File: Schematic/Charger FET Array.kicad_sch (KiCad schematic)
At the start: 31 parts, among them Q21 CSD19531Q5A, Q22 CSD19531Q5A, Q23 CSD19531Q5A, Q24 CSD19531Q5A

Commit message: added sensors?
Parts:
- renumbered C71 to C126, C70 to C127, C69 to C128, C73 to C129, C72 to C130, C74 to C131, C75 to C132, C76 to C133, C77 to C134, C78 to C135, C79 to C136, L1 to L2, Q21 to Q27, Q22 to Q28, Q24 to Q29, Q23 to Q30, R99 to R114, R98 to R115, R97 to R116, R101 to R117, R100 to R118, R102 to R119, R103 to R120, R104 to R121, R105 to R122, R106 to R123, R108 to R124, R107 to R125, R110 to R126, R111 to R127, R112 to R128

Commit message: 1st Schematic Review
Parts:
- renumbered C126 to C129, C127 to C130, C128 to C131, C129 to C132, C130 to C133, C131 to C134, C132 to C135, C133 to C136, C134 to C137, C135 to C138, C136 to C139, R114 to R116, R115 to R117, R116 to R118, R117 to R119, R118 to R120, R119 to R121, R120 to R122, R121 to R123, R122 to R124, R123 to R125, R124 to R126, R125 to R127, R126 to R128, R127 to R129, R128 to R130

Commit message: updates
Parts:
- renumbered C129 to C130, C130 to C131, C131 to C132, C132 to C133, C133 to C134, C134 to C135, C135 to C136, C136 to C137, C137 to C138, C138 to C139, C139 to C140, R116 to R125, R117 to R126, R118 to R127, R119 to R128, R120 to R129, R121 to R130, R122 to R131, R123 to R132, R124 to R133, R125 to R134, R126 to R135, R127 to R136, R128 to R137, R129 to R138, R130 to R139

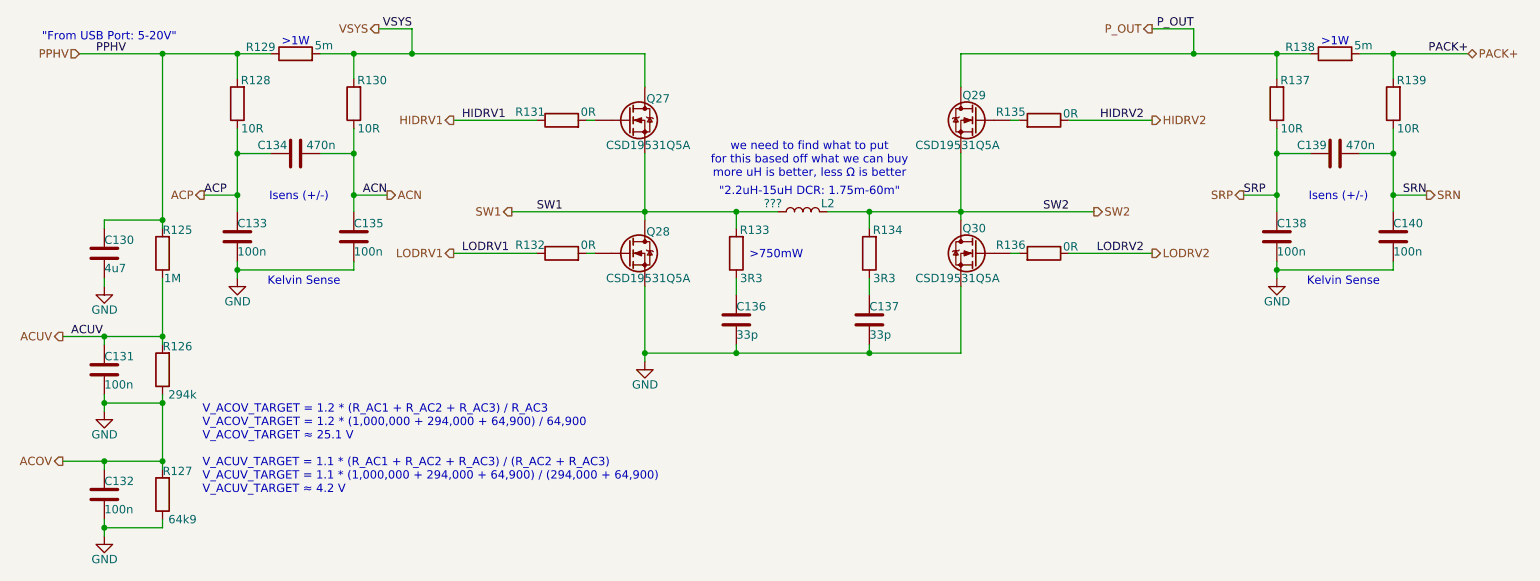
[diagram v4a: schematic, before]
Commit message: updated fuel guage
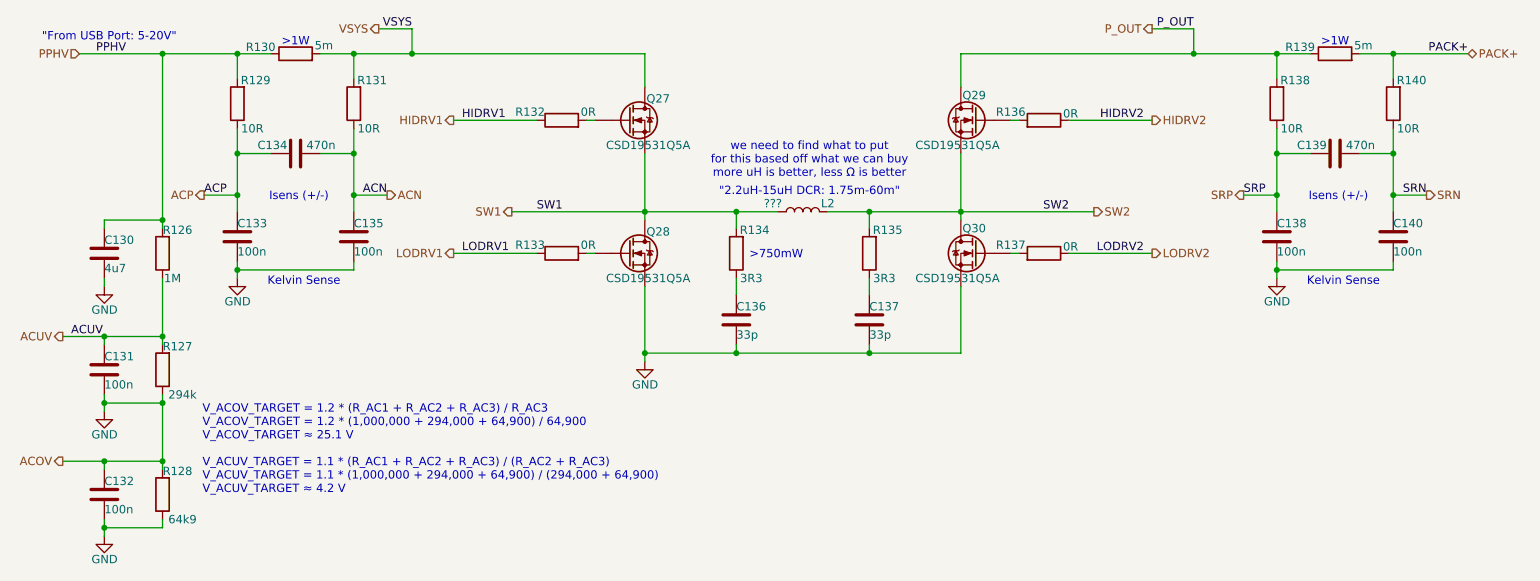
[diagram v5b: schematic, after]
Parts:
- renumbered R125 to R126, R126 to R127, R127 to R128, R128 to R129, R129 to R130, R130 to R131, R131 to R132, R132 to R133, R133 to R134, R134 to R135, R135 to R136, R136 to R137, R137 to R138, R138 to R139, R139 to R140
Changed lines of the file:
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@@
 		(on_board yes)
 		(dnp no)
-		(property "Reference" "R137"
+		(property "Reference" "R138"
 			(at 214.884 87.884 0)
 			(effects
@@
 			(project "STAR"
 				(path "/fc8533bc-25dd-4c20-9b4c-ffebebd6739b/ec72a35b-e7f2-4422-8859-60e9fb848154/9fb42b36-af5a-430a-ae71-09fe6d8fbe9c"
-					(reference "R137")
+					(reference "R138")
 					(unit 1)
 				)
@@
 		(on_board yes)
 		(dnp no)
-		(property "Reference" "R131"
+		(property "Reference" "R132"
 			(at 98.044 92.71 90)
 			(effects
@@
 			(project "STAR"
 				(path "/fc8533bc-25dd-4c20-9b4c-ffebebd6739b/ec72a35b-e7f2-4422-8859-60e9fb848154/9fb42b36-af5a-430a-ae71-09fe6d8fbe9c"
-					(reference "R131")
+					(reference "R132")
 					(unit 1)
 				)
@@
 		(on_board yes)
 		(dnp no)
-		(property "Reference" "R126"
+		(property "Reference" "R127"
 			(at 44.196 128.524 0)
 			(effects
@@
 			(project "STAR"
 				(path "/fc8533bc-25dd-4c20-9b4c-ffebebd6739b/ec72a35b-e7f2-4422-8859-60e9fb848154/9fb42b36-af5a-430a-ae71-09fe6d8fbe9c"
-					(reference "R126")
+					(reference "R127")
 					(unit 1)
 				)
@@
 		(on_board yes)
 		(dnp no)
-		(property "Reference" "R128"
+		(property "Reference" "R129"
 			(at 56.134 87.884 0)
 			(effects
@@
 			(project "STAR"
 				(path "/fc8533bc-25dd-4c20-9b4c-ffebebd6739b/ec72a35b-e7f2-4422-8859-60e9fb848154/9fb42b36-af5a-430a-ae71-09fe6d8fbe9c"
-					(reference "R128")
+					(reference "R129")
 					(unit 1)
 				)
@@
 		(on_board yes)
 		(dnp no)
-		(property "Reference" "R127"
+		(property "Reference" "R128"
 			(at 44.196 147.574 0)
 			(effects
@@
 			(project "STAR"
 				(path "/fc8533bc-25dd-4c20-9b4c-ffebebd6739b/ec72a35b-e7f2-4422-8859-60e9fb848154/9fb42b36-af5a-430a-ae71-09fe6d8fbe9c"
-					(reference "R127")
+					(reference "R128")
 					(unit 1)
 				)
@@
 		(on_board yes)
 		(dnp no)
-		(property "Reference" "R139"
+		(property "Reference" "R140"
 			(at 232.664 87.884 0)
 			(effects
@@
 			(project "STAR"
 				(path "/fc8533bc-25dd-4c20-9b4c-ffebebd6739b/ec72a35b-e7f2-4422-8859-60e9fb848154/9fb42b36-af5a-430a-ae71-09fe6d8fbe9c"
-					(reference "R139")
+					(reference "R140")
 					(unit 1)
 				)
@@
 		(on_board yes)
 		(dnp no)
-		(property "Reference" "R130"
+		(property "Reference" "R131"
 			(at 73.914 87.884 0)
 			(effects
@@
 			(project "STAR"
 				(path "/fc8533bc-25dd-4c20-9b4c-ffebebd6739b/ec72a35b-e7f2-4422-8859-60e9fb848154/9fb42b36-af5a-430a-ae71-09fe6d8fbe9c"
-					(reference "R130")
+					(reference "R131")
 					(unit 1)
 				)
@@
 		(on_board yes)
 		(dnp no)
-		(property "Reference" "R135"
+		(property "Reference" "R136"
 			(at 171.45 92.71 90)
 			(effects
@@
 			(project "STAR"
 				(path "/fc8533bc-25dd-4c20-9b4c-ffebebd6739b/ec72a35b-e7f2-4422-8859-60e9fb848154/9fb42b36-af5a-430a-ae71-09fe6d8fbe9c"
-					(reference "R135")
+					(reference "R136")
 					(unit 1)
 				)
@@
 		(on_board yes)
 		(dnp no)
-		(property "Reference" "R138"
+		(property "Reference" "R139"
 			(at 215.646 82.804 90)
 			(effects
@@
 			(project "STAR"
 				(path "/fc8533bc-25dd-4c20-9b4c-ffebebd6739b/ec72a35b-e7f2-4422-8859-60e9fb848154/9fb42b36-af5a-430a-ae71-09fe6d8fbe9c"
-					(reference "R138")
+					(reference "R139")
 					(unit 1)
 				)
@@
 		(on_board yes)
 		(dnp no)
-		(property "Reference" "R129"
+		(property "Reference" "R130"
 			(at 56.896 82.804 90)
 			(effects
@@
 			(project "STAR"
 				(path "/fc8533bc-25dd-4c20-9b4c-ffebebd6739b/ec72a35b-e7f2-4422-8859-60e9fb848154/9fb42b36-af5a-430a-ae71-09fe6d8fbe9c"
-					(reference "R129")
+					(reference "R130")
 					(unit 1)
 				)
@@
 		(on_board yes)
 		(dnp no)
-		(property "Reference" "R133"
+		(property "Reference" "R134"
 			(at 132.334 110.744 0)
 			(effects
@@
 			(project "STAR"
 				(path "/fc8533bc-25dd-4c20-9b4c-ffebebd6739b/ec72a35b-e7f2-4422-8859-60e9fb848154/9fb42b36-af5a-430a-ae71-09fe6d8fbe9c"
-					(reference "R133")
+					(reference "R134")
 					(unit 1)
 				)
@@
 		(on_board yes)
 		(dnp no)
-		(property "Reference" "R125"
+		(property "Reference" "R126"
 			(at 44.196 110.744 0)
 			(effects
@@
 			(project "STAR"
 				(path "/fc8533bc-25dd-4c20-9b4c-ffebebd6739b/ec72a35b-e7f2-4422-8859-60e9fb848154/9fb42b36-af5a-430a-ae71-09fe6d8fbe9c"
-					(reference "R125")
+					(reference "R126")
 					(unit 1)
 				)
@@
 		(on_board yes)
 		(dnp no)
-		(property "Reference" "R134"
+		(property "Reference" "R135"
 			(at 152.654 110.744 0)
 			(effects
@@
 			(project "STAR"
 				(path "/fc8533bc-25dd-4c20-9b4c-ffebebd6739b/ec72a35b-e7f2-4422-8859-60e9fb848154/9fb42b36-af5a-430a-ae71-09fe6d8fbe9c"
-					(reference "R134")
+					(reference "R135")
 					(unit 1)
 				)
@@
 		(on_board yes)
 		(dnp no)
-		(property "Reference" "R132"
+		(property "Reference" "R133"
 			(at 98.044 113.03 90)
 			(effects
@@
 			(project "STAR"
 				(path "/fc8533bc-25dd-4c20-9b4c-ffebebd6739b/ec72a35b-e7f2-4422-8859-60e9fb848154/9fb42b36-af5a-430a-ae71-09fe6d8fbe9c"
-					(reference "R132")
+					(reference "R133")
 					(unit 1)
 				)
@@
 		(on_board yes)
 		(dnp no)
-		(property "Reference" "R136"
+		(property "Reference" "R137"
 			(at 171.45 113.03 90)
 			(effects
@@
 			(project "STAR"
 				(path "/fc8533bc-25dd-4c20-9b4c-ffebebd6739b/ec72a35b-e7f2-4422-8859-60e9fb848154/9fb42b36-af5a-430a-ae71-09fe6d8fbe9c"
-					(reference "R136")
+					(reference "R137")
 					(unit 1)
 				)

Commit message: Added MCU
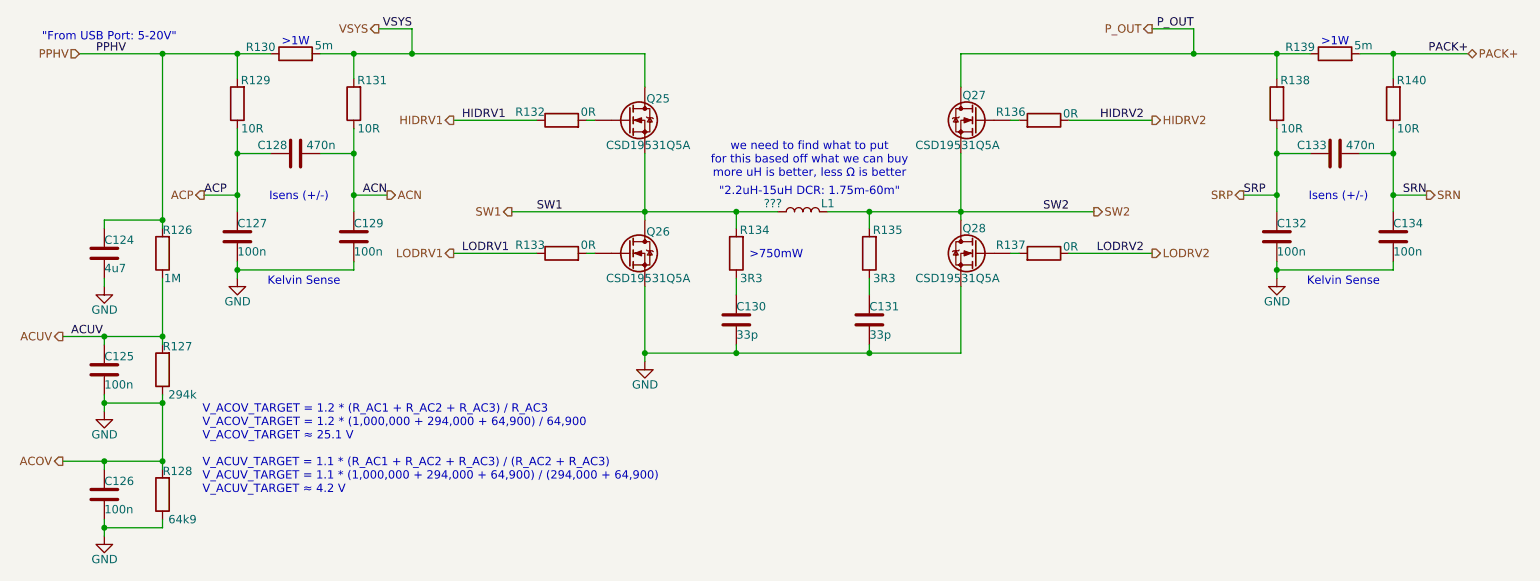
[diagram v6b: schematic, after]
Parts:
- renumbered C130 to C124, C131 to C125, C132 to C126, C133 to C127, C134 to C128, C135 to C129, C136 to C130, C137 to C131, C138 to C132, C139 to C133, C140 to C134, L2 to L1, Q27 to Q25, Q28 to Q26, Q29 to Q27, Q30 to Q28
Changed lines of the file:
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@@
 		(on_board yes)
 		(dnp no)
-		(property "Reference" "C137"
+		(property "Reference" "C131"
 			(at 149.86 122.428 0)
 			(effects
@@
 			(project "STAR"
 				(path "/fc8533bc-25dd-4c20-9b4c-ffebebd6739b/ec72a35b-e7f2-4422-8859-60e9fb848154/9fb42b36-af5a-430a-ae71-09fe6d8fbe9c"
-					(reference "C137")
+					(reference "C131")
 					(unit 1)
 				)
@@
 		(on_board yes)
 		(dnp no)
-		(property "Reference" "C132"
+		(property "Reference" "C126"
 			(at 33.02 149.098 0)
 			(effects
@@
 			(project "STAR"
 				(path "/fc8533bc-25dd-4c20-9b4c-ffebebd6739b/ec72a35b-e7f2-4422-8859-60e9fb848154/9fb42b36-af5a-430a-ae71-09fe6d8fbe9c"
-					(reference "C132")
+					(reference "C126")
 					(unit 1)
 				)
@@
 		(on_board yes)
 		(dnp no)
-		(property "Reference" "#PWR073"
+		(property "Reference" "#PWR076"
 			(at 53.34 124.46 0)
 			(effects
@@
 			(project "STAR"
 				(path "/fc8533bc-25dd-4c20-9b4c-ffebebd6739b/ec72a35b-e7f2-4422-8859-60e9fb848154/9fb42b36-af5a-430a-ae71-09fe6d8fbe9c"
-					(reference "#PWR073")
+					(reference "#PWR076")
 					(unit 1)
 				)
@@
 		(on_board yes)
 		(dnp no)
-		(property "Reference" "L2"
+		(property "Reference" "L1"
 			(at 143.51 106.68 90)
 			(effects
@@
 			(project ""
 				(path "/fc8533bc-25dd-4c20-9b4c-ffebebd6739b/ec72a35b-e7f2-4422-8859-60e9fb848154/9fb42b36-af5a-430a-ae71-09fe6d8fbe9c"
-					(reference "L2")
+					(reference "L1")
 					(unit 1)
 				)
@@
 		(on_board yes)
 		(dnp no)
-		(property "Reference" "C136"
+		(property "Reference" "C130"
 			(at 129.54 122.428 0)
 			(effects
@@
 			(project "STAR"
 				(path "/fc8533bc-25dd-4c20-9b4c-ffebebd6739b/ec72a35b-e7f2-4422-8859-60e9fb848154/9fb42b36-af5a-430a-ae71-09fe6d8fbe9c"
-					(reference "C136")
+					(reference "C130")
 					(unit 1)
 				)
@@
 		(on_board yes)
 		(dnp no)
-		(property "Reference" "C134"
+		(property "Reference" "C128"
 			(at 60.96 97.79 90)
 			(effects
@@
 			(project "STAR"
 				(path "/fc8533bc-25dd-4c20-9b4c-ffebebd6739b/ec72a35b-e7f2-4422-8859-60e9fb848154/9fb42b36-af5a-430a-ae71-09fe6d8fbe9c"
-					(reference "C134")
+					(reference "C128")
 					(unit 1)
 				)
@@
 		(on_board yes)
 		(dnp no)
-		(property "Reference" "#PWR074"
+		(property "Reference" "#PWR077"
 			(at 115.57 137.16 0)
 			(effects
@@
 			(project "STAR"
 				(path "/fc8533bc-25dd-4c20-9b4c-ffebebd6739b/ec72a35b-e7f2-4422-8859-60e9fb848154/9fb42b36-af5a-430a-ae71-09fe6d8fbe9c"
-					(reference "#PWR074")
+					(reference "#PWR077")
 					(unit 1)
 				)
@@
 		(on_board yes)
 		(dnp no)
-		(property "Reference" "Q28"
+		(property "Reference" "Q26"
 			(at 117.602 110.998 0)
 			(effects
@@
 			(project "STAR"
 				(path "/fc8533bc-25dd-4c20-9b4c-ffebebd6739b/ec72a35b-e7f2-4422-8859-60e9fb848154/9fb42b36-af5a-430a-ae71-09fe6d8fbe9c"
-					(reference "Q28")
+					(reference "Q26")
 					(unit 1)
 				)
@@
 		(on_board yes)
 		(dnp no)
-		(property "Reference" "C135"
+		(property "Reference" "C129"
 			(at 71.12 109.728 0)
 			(effects
@@
 			(project "STAR"
 				(path "/fc8533bc-25dd-4c20-9b4c-ffebebd6739b/ec72a35b-e7f2-4422-8859-60e9fb848154/9fb42b36-af5a-430a-ae71-09fe6d8fbe9c"
-					(reference "C135")
+					(reference "C129")
 					(unit 1)
 				)
@@
 		(on_board yes)
 		(dnp no)
-		(property "Reference" "Q29"
+		(property "Reference" "Q27"
 			(at 165.862 90.17 0)
 			(effects
@@
 			(project "STAR"
 				(path "/fc8533bc-25dd-4c20-9b4c-ffebebd6739b/ec72a35b-e7f2-4422-8859-60e9fb848154/9fb42b36-af5a-430a-ae71-09fe6d8fbe9c"
-					(reference "Q29")
+					(reference "Q27")
 					(unit 1)
 				)
@@
 		(on_board yes)
 		(dnp no)
-		(property "Reference" "C140"
+		(property "Reference" "C134"
 			(at 229.87 109.728 0)
 			(effects
@@
 			(project "STAR"
 				(path "/fc8533bc-25dd-4c20-9b4c-ffebebd6739b/ec72a35b-e7f2-4422-8859-60e9fb848154/9fb42b36-af5a-430a-ae71-09fe6d8fbe9c"
-					(reference "C140")
+					(reference "C134")
 					(unit 1)
 				)
@@
 		(on_board yes)
 		(dnp no)
-		(property "Reference" "Q27"
+		(property "Reference" "Q25"
 			(at 117.602 90.678 0)
 			(effects
@@
 			(project "STAR"
 				(path "/fc8533bc-25dd-4c20-9b4c-ffebebd6739b/ec72a35b-e7f2-4422-8859-60e9fb848154/9fb42b36-af5a-430a-ae71-09fe6d8fbe9c"
-					(reference "Q27")
+					(reference "Q25")
 					(unit 1)
 				)
@@
 		(on_board yes)
 		(dnp no)
-		(property "Reference" "Q30"
+		(property "Reference" "Q28"
 			(at 165.862 110.49 0)
 			(effects
@@
 			(project "STAR"
 				(path "/fc8533bc-25dd-4c20-9b4c-ffebebd6739b/ec72a35b-e7f2-4422-8859-60e9fb848154/9fb42b36-af5a-430a-ae71-09fe6d8fbe9c"
-					(reference "Q30")
+					(reference "Q28")
 					(unit 1)
 				)
@@
 		(on_board yes)
 		(dnp no)
-		(property "Reference" "#PWR071"
+		(property "Reference" "#PWR074"
 			(at 33.02 144.78 0)
 			(effects
@@
 			(project "STAR"
 				(path "/fc8533bc-25dd-4c20-9b4c-ffebebd6739b/ec72a35b-e7f2-4422-8859-60e9fb848154/9fb42b36-af5a-430a-ae71-09fe6d8fbe9c"
-					(reference "#PWR071")
+					(reference "#PWR074")
 					(unit 1)
 				)
@@
 		(on_board yes)
 		(dnp no)
-		(property "Reference" "#PWR075"
+		(property "Reference" "#PWR078"
 			(at 212.09 124.46 0)
 			(effects
@@
 			(project "STAR"
 				(path "/fc8533bc-25dd-4c20-9b4c-ffebebd6739b/ec72a35b-e7f2-4422-8859-60e9fb848154/9fb42b36-af5a-430a-ae71-09fe6d8fbe9c"
-					(reference "#PWR075")
+					(reference "#PWR078")
 					(unit 1)
 				)
@@
 		(on_board yes)
 		(dnp no)
-		(property "Reference" "#PWR072"
+		(property "Reference" "#PWR075"
 			(at 33.02 163.83 0)
 			(effects
@@
 			(project "STAR"
 				(path "/fc8533bc-25dd-4c20-9b4c-ffebebd6739b/ec72a35b-e7f2-4422-8859-60e9fb848154/9fb42b36-af5a-430a-ae71-09fe6d8fbe9c"
-					(reference "#PWR072")
+					(reference "#PWR075")
 					(unit 1)
 				)
@@
 		(on_board yes)
 		(dnp no)
-		(property "Reference" "C133"
+		(property "Reference" "C127"
 			(at 53.34 109.728 0)
 			(effects
@@
 			(project "STAR"
 				(path "/fc8533bc-25dd-4c20-9b4c-ffebebd6739b/ec72a35b-e7f2-4422-8859-60e9fb848154/9fb42b36-af5a-430a-ae71-09fe6d8fbe9c"
-					(reference "C133")
+					(reference "C127")
 					(unit 1)
 				)
@@
 		(on_board yes)
 		(dnp no)
-		(property "Reference" "C131"
+		(property "Reference" "C125"
 			(at 33.02 130.048 0)
 			(effects
@@
 			(project "STAR"
 				(path "/fc8533bc-25dd-4c20-9b4c-ffebebd6739b/ec72a35b-e7f2-4422-8859-60e9fb848154/9fb42b36-af5a-430a-ae71-09fe6d8fbe9c"
-					(reference "C131")
+					(reference "C125")
 					(unit 1)
 				)
@@
 		(on_board yes)
 		(dnp no)
-		(property "Reference" "C130"
+		(property "Reference" "C124"
 			(at 33.02 112.268 0)
 			(effects
@@
 			(project "STAR"
 				(path "/fc8533bc-25dd-4c20-9b4c-ffebebd6739b/ec72a35b-e7f2-4422-8859-60e9fb848154/9fb42b36-af5a-430a-ae71-09fe6d8fbe9c"
-					(reference "C130")
+					(reference "C124")
 					(unit 1)
 				)
@@
 		(on_board yes)
 		(dnp no)
-		(property "Reference" "C138"
+		(property "Reference" "C132"
 			(at 212.09 109.728 0)
 			(effects
@@
 			(project "STAR"
 				(path "/fc8533bc-25dd-4c20-9b4c-ffebebd6739b/ec72a35b-e7f2-4422-8859-60e9fb848154/9fb42b36-af5a-430a-ae71-09fe6d8fbe9c"
-					(reference "C138")
+					(reference "C132")
 					(unit 1)
 				)
@@
 		(on_board yes)
 		(dnp no)
-		(property "Reference" "#PWR070"
+		(property "Reference" "#PWR073"
 			(at 33.02 125.73 0)
 			(effects
@@
 			(project "STAR"
 				(path "/fc8533bc-25dd-4c20-9b4c-ffebebd6739b/ec72a35b-e7f2-4422-8859-60e9fb848154/9fb42b36-af5a-430a-ae71-09fe6d8fbe9c"
-					(reference "#PWR070")
+					(reference "#PWR073")
 					(unit 1)
 				)
@@
 		(on_board yes)
 		(dnp no)
-		(property "Reference" "C139"
+		(property "Reference" "C133"
 			(at 219.71 97.79 90)
 			(effects
@@
 			(project "STAR"
 				(path "/fc8533bc-25dd-4c20-9b4c-ffebebd6739b/ec72a35b-e7f2-4422-8859-60e9fb848154/9fb42b36-af5a-430a-ae71-09fe6d8fbe9c"
-					(reference "C139")
+					(reference "C133")
 					(unit 1)
 				)

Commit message: Started to work on the BOM
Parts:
- C123: renamed from C124; footprint (none) -> Capacitor_SMD:C_1206_3216Metric_Pad1.33x1.80mm_HandSolder; Link (none) -> https://mou.sr/45jYGQI; Manufacturer Part Number (none) -> CL31B475KBHNFNE; Price per Unit (none) -> 0.27; Supplier (none) -> Mouser; Supplier Part Number (none) -> 187-CL31B475KBHNFNE
- C124: renamed from C125; footprint (none) -> Capacitor_SMD:C_1206_3216Metric_Pad1.33x1.80mm_HandSolder; Link (none) -> https://mou.sr/4n9ybmQ; Manufacturer Part Number (none) -> CL31B104KBCNNNC; Price per Unit (none) -> 0.11; Supplier (none) -> Mouser; Supplier Part Number (none) -> 187-CL31B104KBCNNNC
- C125: renamed from C126; footprint (none) -> Capacitor_SMD:C_1206_3216Metric_Pad1.33x1.80mm_HandSolder; Link (none) -> https://mou.sr/4n9ybmQ; Manufacturer Part Number (none) -> CL31B104KBCNNNC; Price per Unit (none) -> 0.11; Supplier (none) -> Mouser; Supplier Part Number (none) -> 187-CL31B104KBCNNNC
- C126: renamed from C127; footprint (none) -> Capacitor_SMD:C_1206_3216Metric_Pad1.33x1.80mm_HandSolder; Link (none) -> https://mou.sr/4n9ybmQ; Manufacturer Part Number (none) -> CL31B104KBCNNNC; Price per Unit (none) -> 0.11; Supplier (none) -> Mouser; Supplier Part Number (none) -> 187-CL31B104KBCNNNC
- C127: renamed from C128; footprint (none) -> Capacitor_SMD:C_0805_2012Metric_Pad1.18x1.45mm_HandSolder; Link (none) -> https://mou.sr/47ZiytM; Manufacturer Part Number (none) -> CL21B474KBFNNNG; Price per Unit (none) -> 0.10; Supplier (none) -> Mouser; Supplier Part Number (none) -> 187-CL21B474KBFNNNG
- C128: renamed from C129; footprint (none) -> Capacitor_SMD:C_1206_3216Metric_Pad1.33x1.80mm_HandSolder; Link (none) -> https://mou.sr/4n9ybmQ; Manufacturer Part Number (none) -> CL31B104KBCNNNC; Price per Unit (none) -> 0.11; Supplier (none) -> Mouser; Supplier Part Number (none) -> 187-CL31B104KBCNNNC
- C129: renamed from C130; footprint (none) -> Capacitor_SMD:C_0603_1608Metric_Pad1.08x0.95mm_HandSolder; Link (none) -> https://mou.sr/4nf5STV; Manufacturer Part Number (none) -> CL10C330JB8NNND; Price per Unit (none) -> 0.10; Supplier (none) -> Mouser; Supplier Part Number (none) -> 187-CL10C330JB8NNND
- C130: renamed from C131; footprint (none) -> Capacitor_SMD:C_0603_1608Metric_Pad1.08x0.95mm_HandSolder; Link (none) -> https://mou.sr/4nf5STV; Manufacturer Part Number (none) -> CL10C330JB8NNND; Price per Unit (none) -> 0.10; Supplier (none) -> Mouser; Supplier Part Number (none) -> 187-CL10C330JB8NNND
- C131: renamed from C132; footprint (none) -> Capacitor_SMD:C_1206_3216Metric_Pad1.33x1.80mm_HandSolder; Link (none) -> https://mou.sr/4n9ybmQ; Manufacturer Part Number (none) -> CL31B104KBCNNNC; Price per Unit (none) -> 0.11; Supplier (none) -> Mouser; Supplier Part Number (none) -> 187-CL31B104KBCNNNC
- C132: renamed from C133; footprint (none) -> Capacitor_SMD:C_0805_2012Metric_Pad1.18x1.45mm_HandSolder; Link (none) -> https://mou.sr/47ZiytM; Manufacturer Part Number (none) -> CL21B474KBFNNNG; Price per Unit (none) -> 0.10; Supplier (none) -> Mouser; Supplier Part Number (none) -> 187-CL21B474KBFNNNG
- C133: renamed from C134; footprint (none) -> Capacitor_SMD:C_1206_3216Metric_Pad1.33x1.80mm_HandSolder; Link (none) -> https://mou.sr/4n9ybmQ; Manufacturer Part Number (none) -> CL31B104KBCNNNC; Price per Unit (none) -> 0.11; Supplier (none) -> Mouser; Supplier Part Number (none) -> 187-CL31B104KBCNNNC
- Q25, Q26, Q27, Q28: footprint Package_TO_SOT_SMD:TDSON-8-1 -> (none)
- renumbered R126 to R122, R127 to R123, R128 to R124, R129 to R125, R130 to R126, R131 to R127, R132 to R128, R133 to R129, R134 to R130, R135 to R131, R136 to R132, R137 to R133, R138 to R134, R139 to R135, R140 to R136
